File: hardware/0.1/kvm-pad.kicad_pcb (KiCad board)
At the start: 2 copper layers, 76.2 x 64.1 mm, 96 parts, among them J1 USB_C_Receptacle_USB2.0, J2 USB_C_Receptacle_USB2.0, J3 AVR-ISP-6, J4 USB_A, J5 USB_A, J6 USB_A, K1 KEYSW, K2 KEYSW, K3 KEYSW, K4 KEYSW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

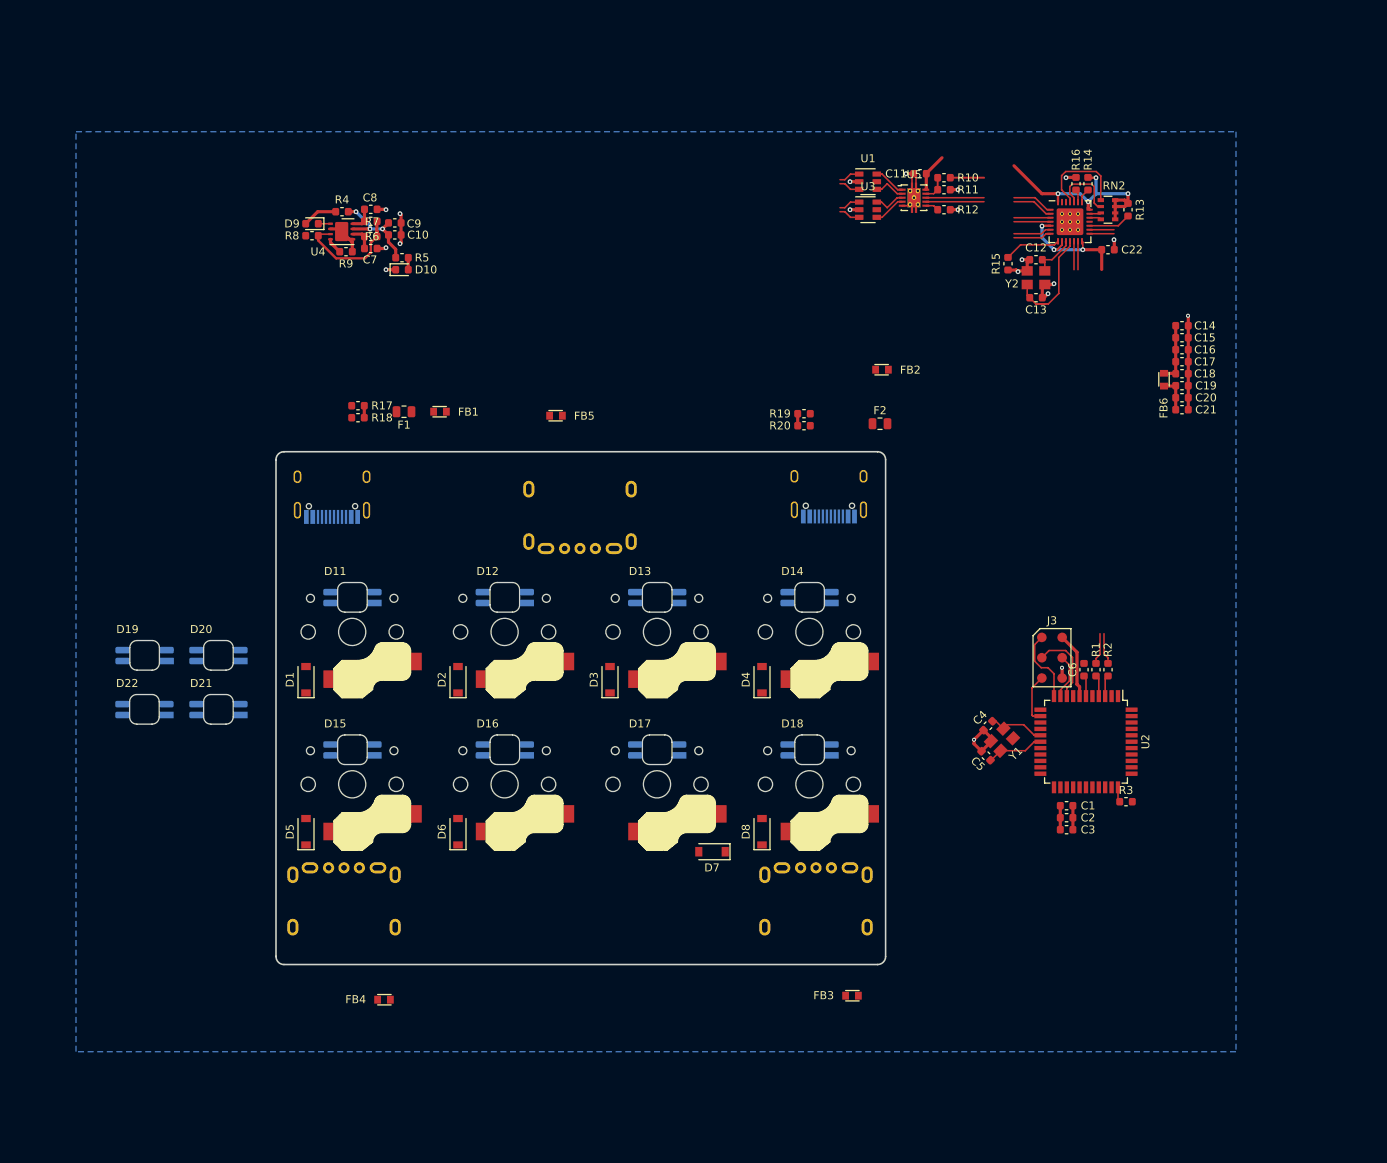
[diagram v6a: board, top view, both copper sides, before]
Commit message: [pcb] Hub routing
Decoupling + crystal are high priority and moved closer to
Also fixed various things
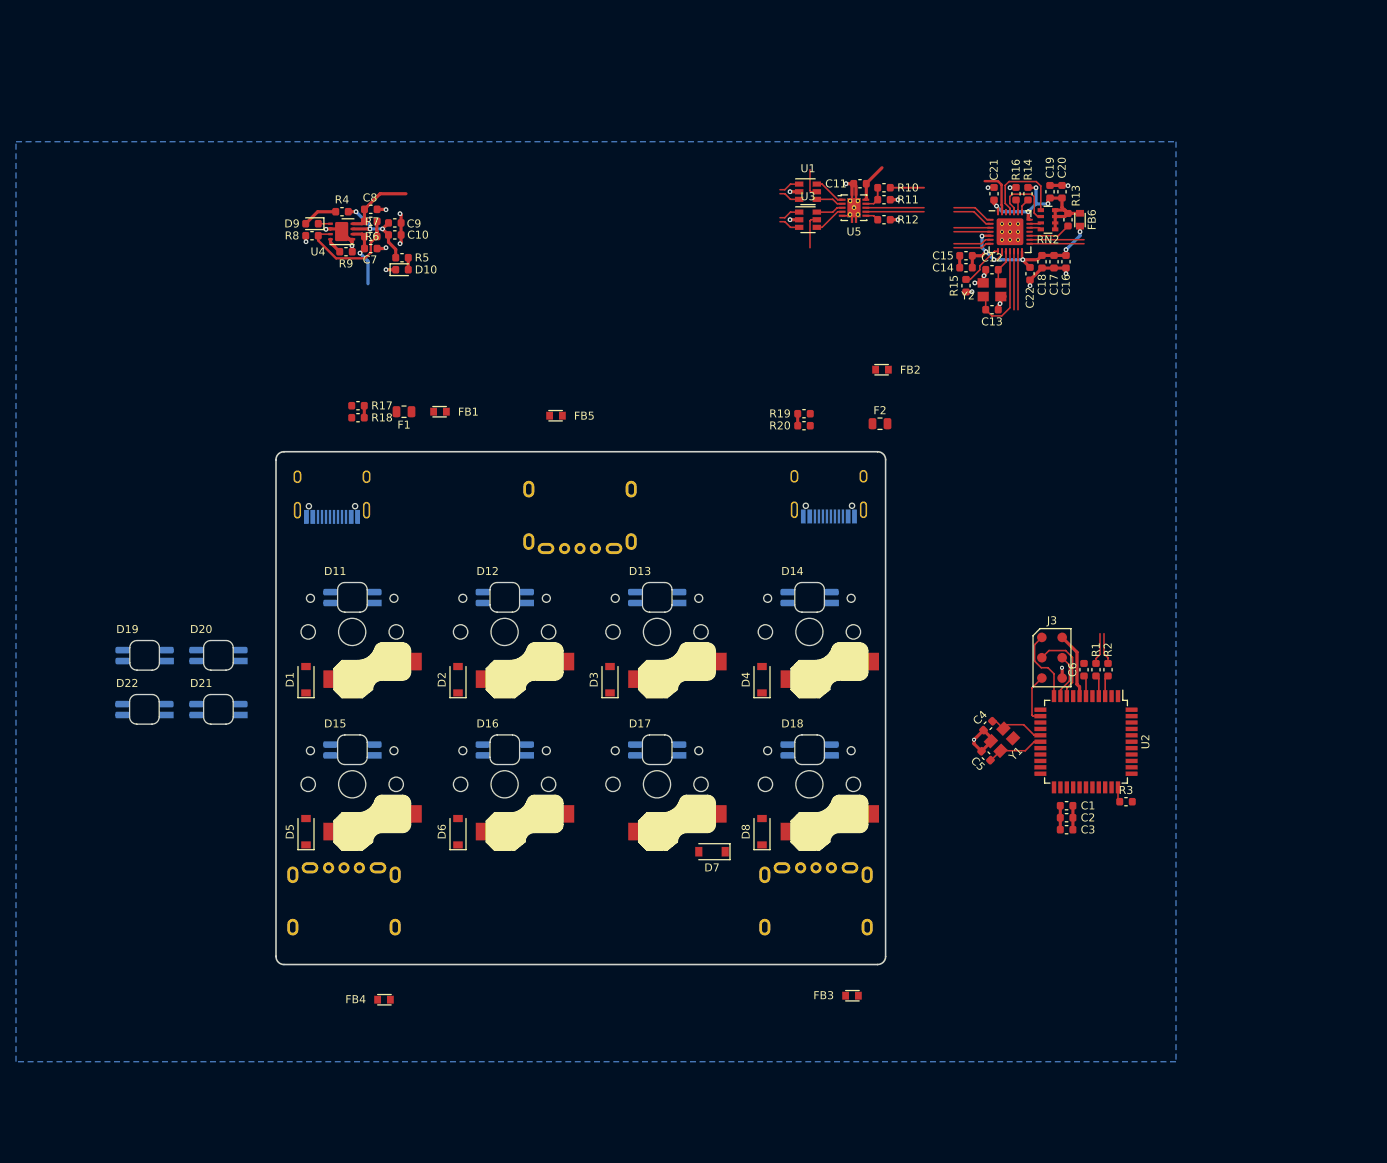
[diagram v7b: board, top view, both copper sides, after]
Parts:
- moved C21 35.8 mm to (89.8, -32.2), turned to 90 degrees
- moved C20 29.8 mm to (98.2, -32.5), turned to 90 degrees
- moved C19 29.3 mm to (96.8, -32.5), turned to 90 degrees
- moved C15 28.9 mm to (86.2, -24.5), turned to 180 degrees
- moved C14 28.0 mm to (86.2, -23.0), turned to 180 degrees
- moved FB6 22.6 mm to (100.5, -29.0), turned to 90 degrees
- moved C18 22.4 mm to (95.8, -23.8), turned to 270 degrees
- moved C17 20.3 mm to (97.2, -23.8), turned to 270 degrees
- moved C16 18.2 mm to (98.8, -23.8), turned to 270 degrees
- moved C22 10.2 mm to (94.2, -22.2), turned to 270 degrees
- moved C11 7.60 mm to (73.0, -33.5)
- moved R10 7.60 mm to (76.0, -33.0)
- moved R11 7.60 mm to (76.0, -31.5)
- moved R12 7.60 mm to (76.0, -29.0)
- moved R13 7.60 mm to (99.0, -29.0)
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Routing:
- net +3V3: track 33.5 -> 25.4 mm
- net /USB_5V_1: track 3.07 -> 9.07 mm
- net +5V: track 24.1 -> 29.9 mm
- net /USB_5V_2: track 3.07 -> 8.12 mm, vias 0 -> 1
- net /USB_VBUS_2: track 0.00 -> 4.28 mm
- net /usb/D3_D-: track 3.55 -> 7.30 mm
- net /usb/D3_D+: track 3.55 -> 7.30 mm
- net /MCU_D-: track 6.97 -> 10.7 mm
- net /MCU_D+: track 6.97 -> 10.7 mm
- net GND: track 60.3 -> 56.6 mm, vias 19 -> 24
- net /USB_VBUS_1: track 0.00 -> 3.53 mm
- net +3.3VA: track 28.0 -> 30.5 mm, vias 3 -> 6
- net /usb/XOUT: track 14.6 -> 12.6 mm
- net /usb/XIN: track 5.99 -> 4.58 mm
- net Net-(R15-Pad1): track 7.08 -> 5.74 mm
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
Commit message: [pcb] Layouting
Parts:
- moved C1 69.1 mm to (37.6, 76.2)
- moved C2 69.1 mm to (37.6, 77.8)
- moved C3 69.1 mm to (37.6, 79.2)
- moved C4 69.1 mm to (27.8, 66.2)
- moved C5 69.1 mm to (27.5, 70.0)
- moved C6 69.1 mm to (39.8, 59.2)
- moved J3 69.1 mm to (35.8, 57.8)
- moved R1 69.1 mm to (41.2, 59.2)
- moved R2 69.1 mm to (42.8, 59.2)
- moved R3 69.1 mm to (45.0, 75.8)
- moved U2 69.1 mm to (40.0, 68.2)
- moved Y1 69.1 mm to (29.5, 68.0)
- moved R10 41.8 mm to (35.8, -21.8), turned to 90 degrees
- moved C11 40.5 mm to (35.2, -18.8), turned to 90 degrees
- moved R11 40.0 mm to (37.2, -21.8), turned to 270 degrees
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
